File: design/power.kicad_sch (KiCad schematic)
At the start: 39 parts, among them J10 PJ-002BH, U4 TPS7A2050PDQN, U5 TPS7A2033PDQN, U6 LMR33630ADDA, U7 LMR33630ADDA

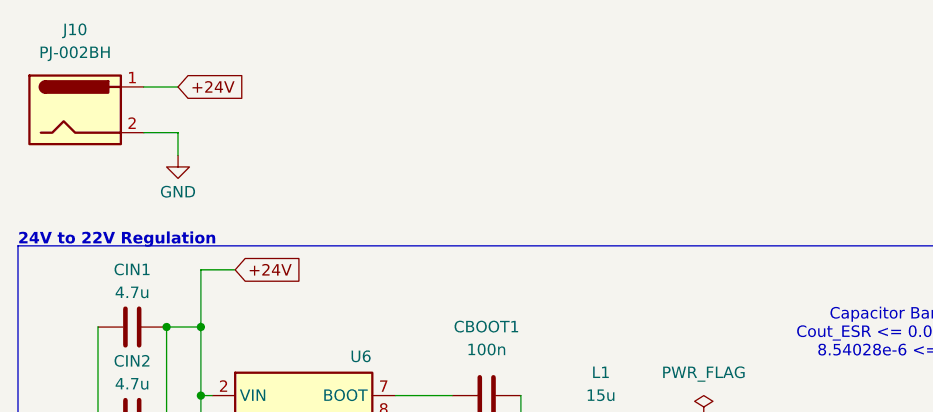
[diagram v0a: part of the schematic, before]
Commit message: Improved power supply filtering and surge protection
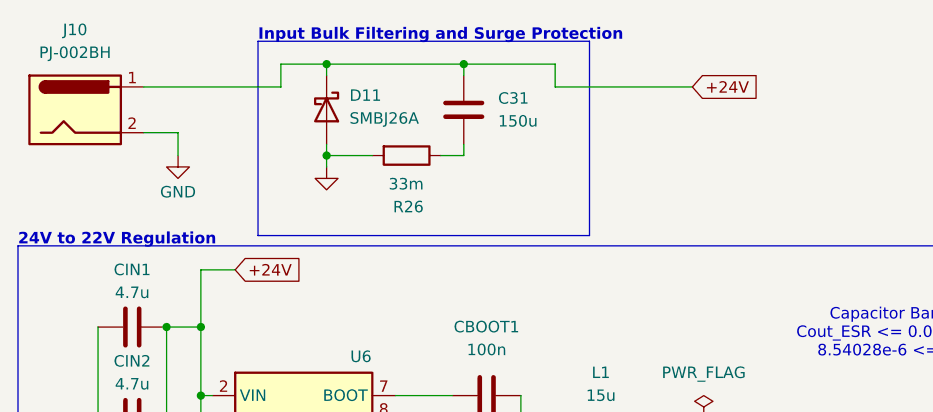
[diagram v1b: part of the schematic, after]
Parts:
- added C31: 150u, Capacitor_THT:C_Radial_D10.0mm_H20.0mm_P5.00mm, symbol Device:C
- added D11: SMBJ26A, Diode_SMD:D_SMB, symbol Device:D_Schottky
- added R26: 33m, Resistor_SMD:R_0603_1608Metric, symbol Device:R
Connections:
- net +24V: now also C31.1, D11.1 (K)
- net GND: now also D11.2 (A), R26.2
- new net: C31.2, R26.1
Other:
- note added: "Input Bulk Filtering and Surge Protection"
